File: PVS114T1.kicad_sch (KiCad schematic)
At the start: 36 parts, among them J1 61FVXS-RSM1-GAN-TF_LF__SN_, U1 BU90T82-ZE2, U2 LT3473

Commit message: Added license to shematic
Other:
- title: PVS114T1_v17.sch -> Sony ECX335BG driver board for rasbery pi.sch
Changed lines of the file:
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@@
   (paper "A0")
   (title_block
-    (title "PVS114T1_v17.sch")
+    (title "Sony ECX335BG driver board for rasbery pi.sch")
     (date "5 JAN 2023")
+    (comment 1 "for compatibility with rasbery pi")
+    (comment 2 "Modified version of https://github.com/aedancullen/sony-ecx")
+    (comment 3 "Lisence : GPL-3.0")
+    (comment 4 "gnu.org/licenses/gpl-3.0")
   )
   (junction (at 822.96 712.47) (diameter 0) (color 0 0 0 0)

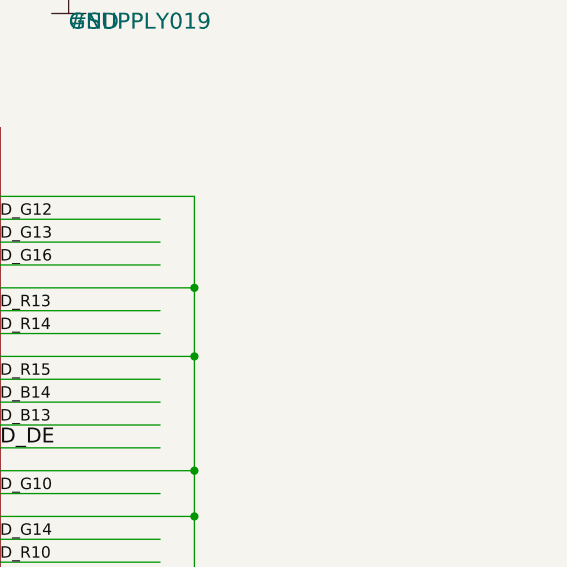
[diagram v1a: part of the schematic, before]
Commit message: Added a pin header for the config pins 	modified:   PVS114T1.kicad_pcb 	modified:   PVS114T1.kicad_prl 	modified:   PVS114T1.kicad_sch
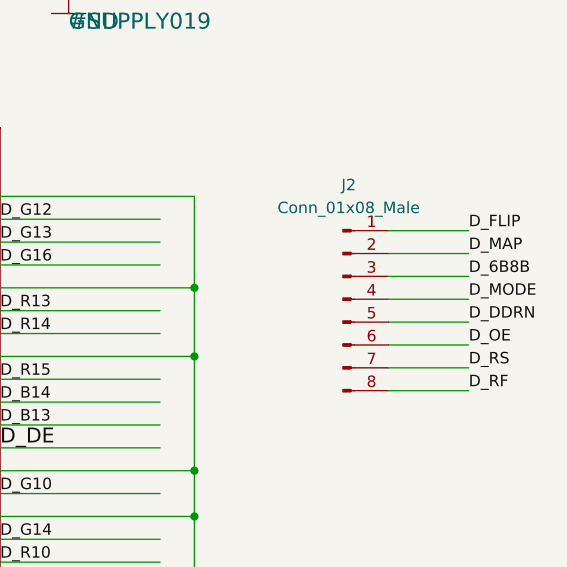
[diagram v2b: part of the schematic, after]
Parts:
- added J2: Conn_01x08_Male, Connector_PinHeader_1.00mm:PinHeader_1x08_P1.00mm_Vertical, symbol Connector:Conn_01x08_Male
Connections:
- net D_6B8B: now also J2.3 (Pin_3)
- net D_DDRN: now also J2.5 (Pin_5)
- net D_FLIP: now also J2.1 (Pin_1)
- net D_MAP: now also J2.2 (Pin_2)
- net D_MODE: now also J2.4 (Pin_4)
- net D_OE: now also J2.6 (Pin_6)
- net D_RF: now also J2.8 (Pin_8)
- net D_RS: now also J2.7 (Pin_7)
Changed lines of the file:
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@@
     (stroke (width 0) (type default) (color 0 0 0 0))
   )
+  (wire (pts (xy 1038.86 769.62) (xy 1047.75 769.62))
+    (stroke (width 0) (type default) (color 0 0 0 0))
+  )
   (wire (pts (xy 782.32 775.97) (xy 769.62 775.97))
     (stroke (width 0) (type default) (color 0 0 0 0))
@@
     (stroke (width 0) (type default) (color 0 0 0 0))
   )
+  (wire (pts (xy 1038.86 774.7) (xy 1047.75 774.7))
+    (stroke (width 0) (type default) (color 0 0 0 0))
+  )
   (wire (pts (xy 966.47 566.42) (xy 966.47 568.96))
     (stroke (width 0) (type default) (color 0 0 0 0))
   )
+  (wire (pts (xy 1038.86 764.54) (xy 1047.75 764.54))
+    (stroke (width 0) (type default) (color 0 0 0 0))
+  )
   (wire (pts (xy 822.96 740.41) (xy 822.96 745.49))
     (stroke (width 0) (type default) (color 0 0 0 0))
@@
     (stroke (width 0) (type default) (color 0 0 0 0))
   )
+  (wire (pts (xy 1038.86 772.16) (xy 1047.75 772.16))
+    (stroke (width 0) (type default) (color 0 0 0 0))
+  )
   (wire (pts (xy 962.66 638.81) (xy 962.66 656.59))
     (stroke (width 0) (type default) (color 0 0 0 0))
@@
     (stroke (width 0) (type default) (color 0 0 0 0))
   )
+  (wire (pts (xy 1038.86 779.78) (xy 1047.75 779.78))
+    (stroke (width 0) (type default) (color 0 0 0 0))
+  )
   (wire (pts (xy 1019.81 669.29) (xy 1027.43 669.29))
     (stroke (width 0) (type default) (color 0 0 0 0))
@@
     (stroke (width 0) (type default) (color 0 0 0 0))
   )
+  (wire (pts (xy 1038.86 767.08) (xy 1047.75 767.08))
+    (stroke (width 0) (type default) (color 0 0 0 0))
+  )
   (wire (pts (xy 966.47 628.65) (xy 974.09 628.65))
     (stroke (width 0) (type default) (color 0 0 0 0))
@@
     (stroke (width 0) (type default) (color 0 0 0 0))
   )
+  (wire (pts (xy 1038.86 762) (xy 1047.75 762))
+    (stroke (width 0) (type default) (color 0 0 0 0))
+  )
   (wire (pts (xy 1019.81 600.71) (xy 1027.43 600.71))
     (stroke (width 0) (type default) (color 0 0 0 0))
@@
     (stroke (width 0) (type default) (color 0 0 0 0))
   )
+  (wire (pts (xy 1038.86 777.24) (xy 1047.75 777.24))
+    (stroke (width 0) (type default) (color 0 0 0 0))
+  )
   (wire (pts (xy 1019.81 623.57) (xy 1027.43 623.57))
     (stroke (width 0) (type default) (color 0 0 0 0))
@@
     (effects (font (size 0.254 0.254)) (justify left bottom))
   )
+  (label "D_RS" (at 1047.75 777.24 0)
+    (effects (font (size 1.27 1.27)) (justify left bottom))
+  )
   (label "D_RF" (at 1019.81 628.65 0)
     (effects (font (size 1.27 1.27)) (justify left bottom))
@@
     (effects (font (size 1.651 1.651)) (justify left bottom))
   )
+  (label "D_MAP" (at 1047.75 764.54 0)
+    (effects (font (size 1.27 1.27)) (justify left bottom))
+  )
   (label "D_R13" (at 995.68 770.89 0)
     (effects (font (size 1.27 1.27)) (justify left bottom))
@@
     (effects (font (size 0.254 0.254)) (justify left bottom))
   )
+  (label "D_OE" (at 1047.75 774.7 0)
+    (effects (font (size 1.27 1.27)) (justify left bottom))
+  )
   (label "N$5" (at 878.84 638.81 90)
     (effects (font (size 0.254 0.254)) (justify left bottom))
@@
     (effects (font (size 1.27 1.27)) (justify left bottom))
   )
+  (label "D_RF" (at 1047.75 779.78 0)
+    (effects (font (size 1.27 1.27)) (justify left bottom))
+  )
   (label "D_CLKIN" (at 965.2 786.13 0)
     (effects (font (size 1.651 1.651)) (justify left bottom))
@@
     (effects (font (size 1.27 1.27)) (justify left bottom))
   )
+  (label "D_FLIP" (at 1047.75 762 0)
+    (effects (font (size 1.27 1.27)) (justify left bottom))
+  )
   (label "GND" (at 999.49 558.8 180)
     (effects (font (size 0.254 0.254)) (justify right bottom))
@@
     (effects (font (size 1.651 1.651)) (justify left bottom))
   )
+  (label "D_MODE" (at 1047.75 769.62 0)
+    (effects (font (size 1.27 1.27)) (justify left bottom))
+  )
   (label "PP1V8_LD1" (at 861.06 750.57 0)
     (effects (font (size 0.254 0.254)) (justify left bottom))
@@
     (effects (font (size 0.254 0.254)) (justify right bottom))
   )
+  (label "D_6B8B" (at 1047.75 767.08 0)
+    (effects (font (size 1.27 1.27)) (justify left bottom))
+  )
   (label "D_B12" (at 984.25 791.21 180)
     (effects (font (size 0.254 0.254)) (justify right bottom))
@@
     (effects (font (size 1.651 1.651)) (justify left bottom))
   )
+  (label "D_DDRN" (at 1047.75 772.16 0)
+    (effects (font (size 1.27 1.27)) (justify left bottom))
+  )
   (label "N$2" (at 830.58 631.19 0)
     (effects (font (size 0.254 0.254)) (justify left bottom))
@@
     (pin "~")
   )
+  (symbol (lib_id "Connector:Conn_01x08_Male") (at 1033.78 769.62 0) (unit 1)
+    (in_bom yes) (on_board yes) (fields_autoplaced)
+    (property "Reference" "J2" (id 0) (at 1034.415 756.92 0))
+    (property "Value" "Conn_01x08_Male" (id 1) (at 1034.415 759.46 0))
+    (property "Footprint" "Connector_PinHeader_1.00mm:PinHeader_1x08_P1.00mm_Vertical" (id 2) (at 1033.78 769.62 0)
+      (effects (font (size 1.27 1.27)) hide)
+    )
+    (property "Datasheet" "~" (id 3) (at 1033.78 769.62 0)
+      (effects (font (size 1.27 1.27)) hide)
+    )
+    (pin "1")
+    (pin "2")
+    (pin "3")
+    (pin "4")
+    (pin "5")
+    (pin "6")
+    (pin "7")
+    (pin "8")
+  )
   (symbol (lib_id "PVS114T1_v17:GND-BAR") (at 966.47 571.5 0) (unit 1)
     (in_bom yes) (on_board yes)
@@
       (reference "J1") (unit 1) (value "61FVXS-RSM1-GAN-TF_LF__SN_") (footprint "61FVXSRSM1GANTFLFSN")
     )
+    (path "/5a50c656-e458-42ed-9140-37a52ce421b4"
+      (reference "J2") (unit 1) (value "Conn_01x08_Male") (footprint "Connector_PinHeader_1.00mm:PinHeader_1x08_P1.00mm_Vertical")
+    )
     (path "/00000000-0000-0000-0000-000063b71805"
